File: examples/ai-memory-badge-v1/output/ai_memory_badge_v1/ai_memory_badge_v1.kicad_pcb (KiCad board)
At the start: 2 copper layers, 68 parts, among them J1 KH-TYPE-C-16P USB-C USB2.0 re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, J2 JST PH 2P SMD battery connect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, J3 U.FL/IPEX antenna connector, J4 UART debug 4P, J5 microSD socket push-push, M1 LCM0827A3038F 3V flat vibrati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, Q1 AO3400A NMOS low-side switch, SW1 Reset tactile switch, SW2 BOOT tactile switch, SW3 Mark tactile switch, SW4 Mute SPDT slide switch, U1 ESP32-S3R8 bare SoC, U2 AP2112K-3.3 600mA LDO, U3 MCP73831 LiPo charger, U4 W25Q128JVSIQ 16MB SPI flash, U5 8MB PSRAM reserve, DNP, U6 USB2.0 ESD protection, U7 I2C secure element, DNP, Y1 40MHz 12pF 10ppm crystal

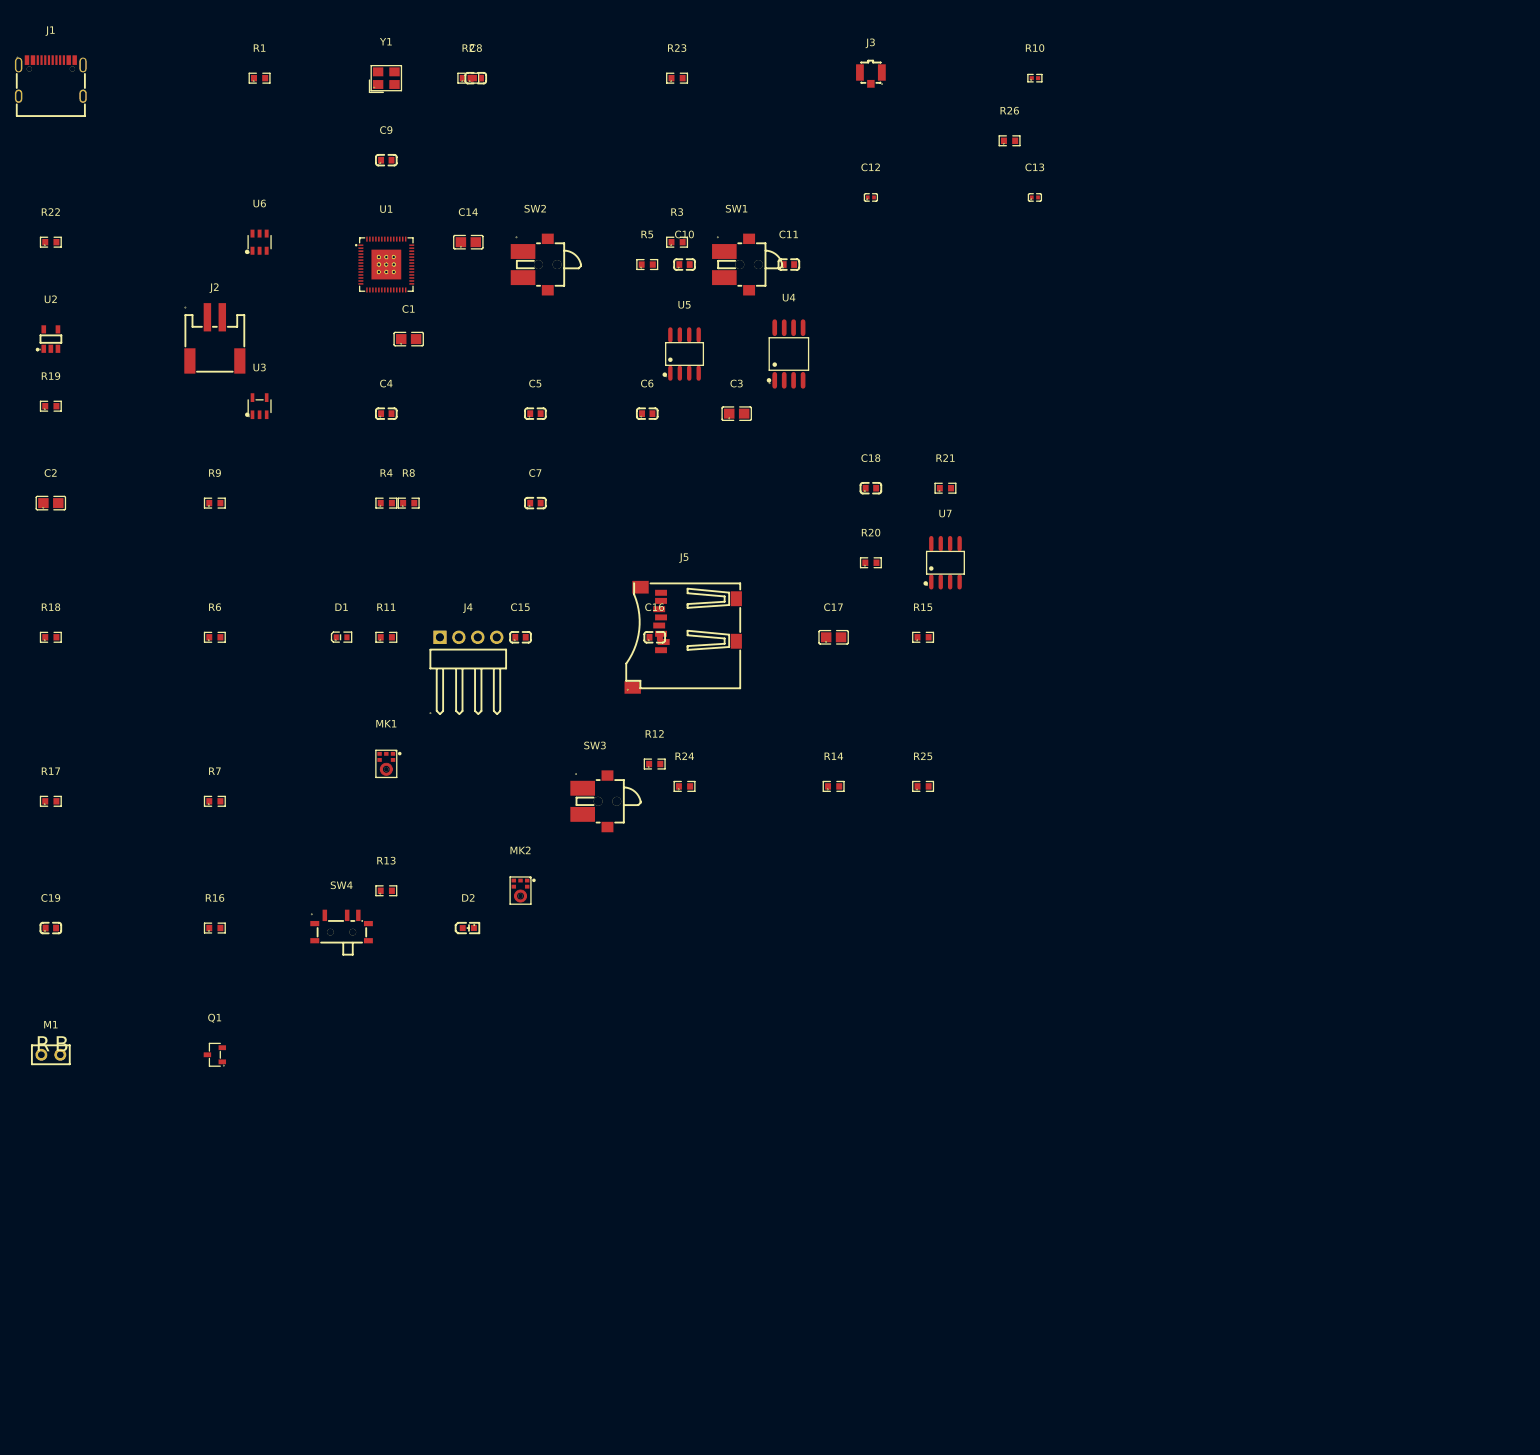
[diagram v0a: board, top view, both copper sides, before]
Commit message: refactor(example): rebuild ai-memory-badge with all topology fixes and optimizations
Circuit fixes:
- LED D1/D2 drive circuit corrected (GPIO controls LED via resistor)
- Mute switch redesigned (SPDT COM directly controls U9.ON)
- SYS_3V3 + EPD_3V3 merged for Rev A (J6.7 direct power)
- Removed J4 UART debug header, SW6 mode button, R16/R32 unused

Design optimizations:
- D3: BAT54C flyback diode across vibration motor M1
- C22: 100nF filter cap on VBAT_SENSE ADC input
- R24/R25: DNP (microSD CMD/DAT0 pullups unused in SPI mode)
- R11: mic power link connected to SYS_3V3
- R27/R28: corrected pullup/pulldown connections
- C20.1/C21.1: removed from SYS_3V3 (was shorting NFC antenna)
- R31.2/R32.2: removed from GND (was shorting button signals)
- J6.7/J7.2: fixed cross-net shorts

BOM consolidation:
- All passives unified to 0603 (was 0603+0805)
- SW4/SW5 unified to SMD SPDT slide switch (MST-12D18G4)
- SW1/SW2 moved to internal test sheet (not user-exposed)

3D models:
- 33 footprint files corrected to ${KIPRJMOD} relative paths
- New 3D models for downloaded components

Co-Authored-By: Claude <noreply@anthropic.com>
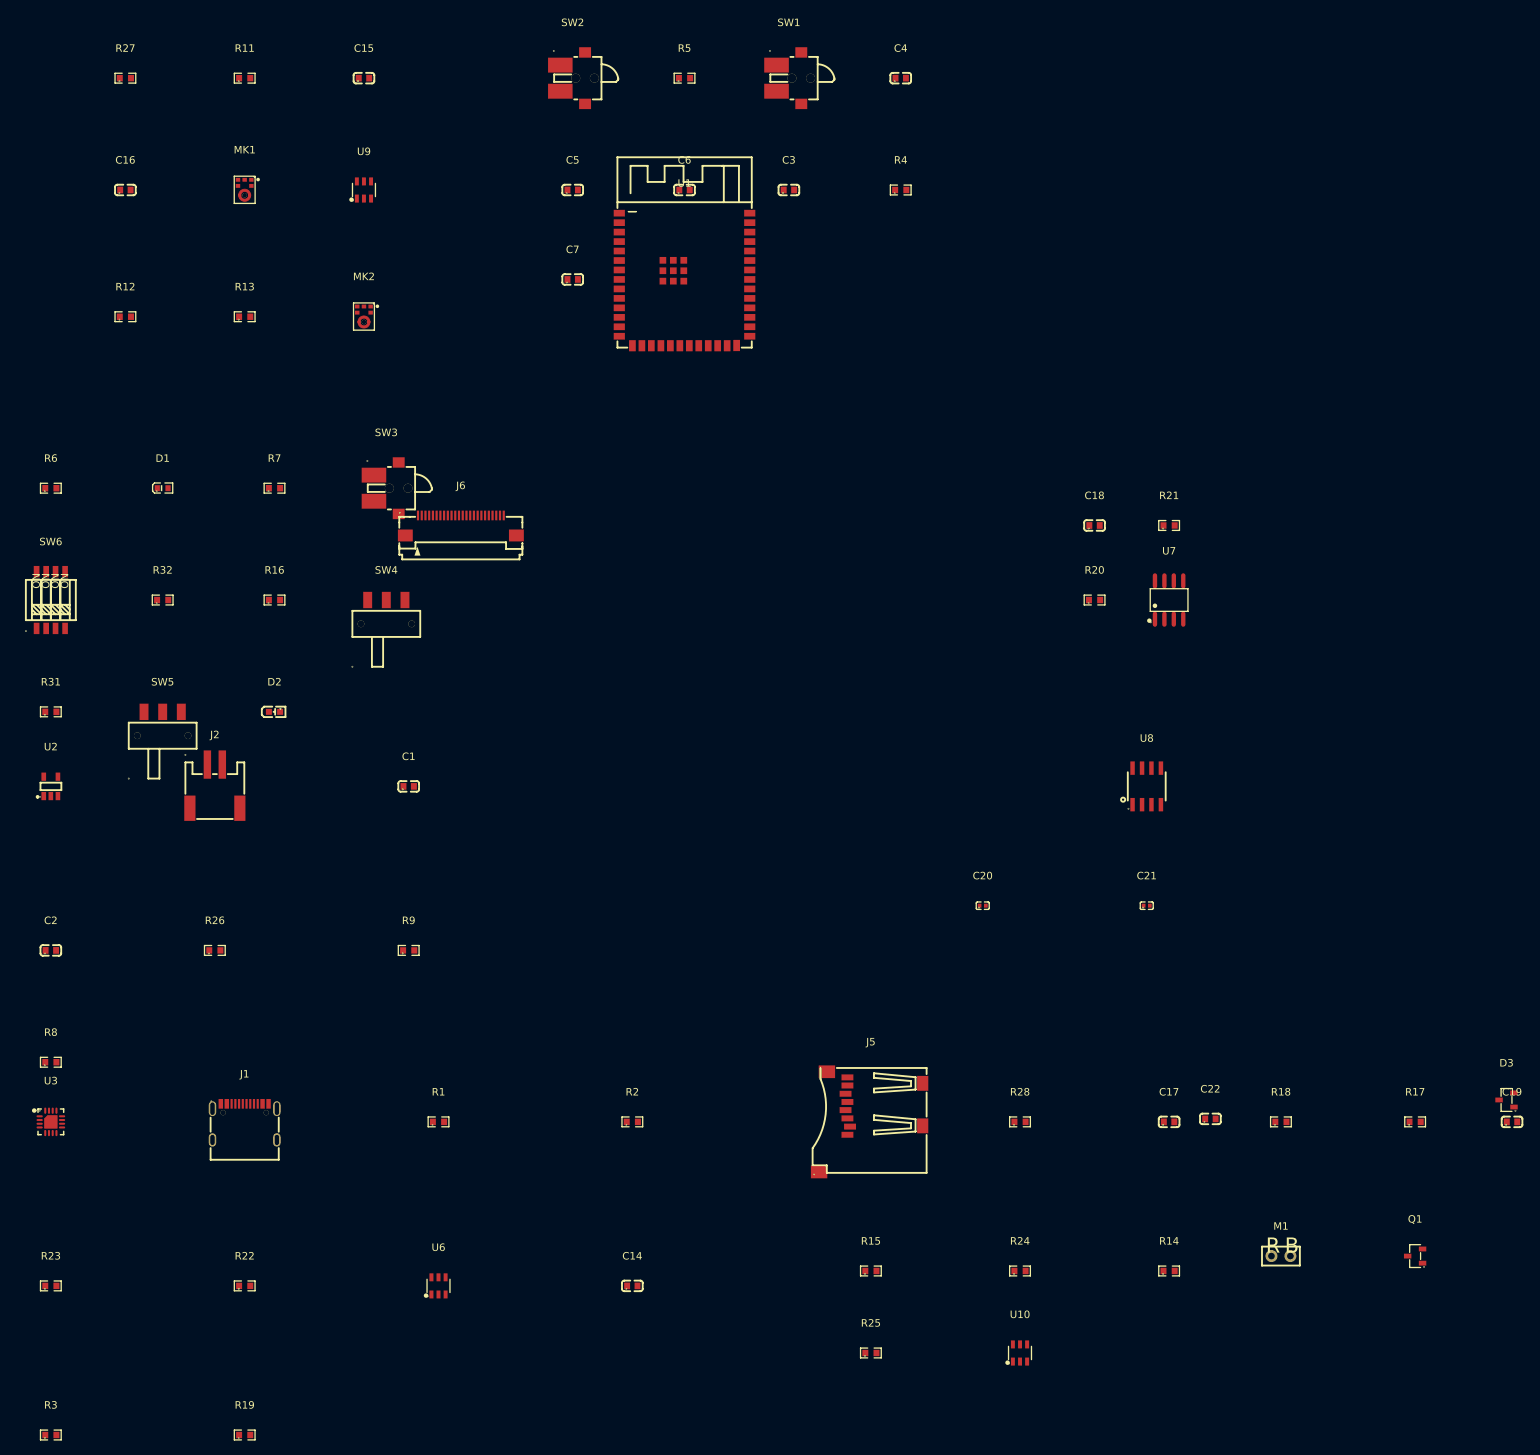
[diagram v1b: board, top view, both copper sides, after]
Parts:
- removed C10, C11: 100nF, C0603
- removed C12, C13: DNP, C0402
- removed C8, C9: 18pF, C0603
- removed J3: U.FL/IPEX antenna connector, RF-SMD_FRF05002-JSS103M
- removed J4: UART debug 4P, HDR-TH_4P-P2.54-H-M-W10.4
- removed R10: 0R, R0402
- removed U4: W25Q128JVSIQ 16MB SPI flash, SOIC-8_L5.3-W5.3-P1.27-LS8.0-BL
- removed U5: 8MB PSRAM reserve, DNP, SOIC-8_L4.9-W3.9-P1.27-LS6.0-BL
- removed Y1: 40MHz 12pF 10ppm crystal, CRYSTAL-SMD_4P-L3.2-W2.5-BL
- added C20: DNP, C0402, F.Cu at (135.0, 121.0)
- added C21: DNP, C0402, F.Cu at (157.0, 121.0)
- added C22: 100nF, C0603, F.Cu at (165.5, 149.6)
- added D3: BAT54 Schottky flyback, SOT-23-3_L2.9-W1.3-P1.90-LS2.4-BR, F.Cu at (205.3, 147.1)
- added J6: 2.13 inch black-white e-paper SPI connector, FPC-SMD_24P-P0.50-L6.1-W16.4, F.Cu at (65.0, 70.0)
- added R27: 10K, R0603, F.Cu at (20.0, 10.0)
- added R28: 100K, R0603, F.Cu at (140.0, 150.0)
- added R31: 10K, R0603, F.Cu at (10.0, 95.0)
- added R32: 10K, R0603, F.Cu at (25.0, 80.0)
- added SW5: REC slide switch SPDT, SW-SMD_MST-12D18G4-SPDT-SLIDE-SWITCH, F.Cu at (25.0, 95.0)
- added SW6: MODE side tactile button, SW-SMD_8P-L6.7-W5.4-P1.27-LS8.4, F.Cu at (10.0, 80.0)
- added U10: TPS22918 SD_3V3 load switch, SOT-23-6_L2.9-W1.6-P0.95-LS2.8-BL, F.Cu at (140.0, 181.0)
- added U8: ST25DV04KC dynamic NFC tag, SO-8_L4.9-W3.9-P1.27-LS6.0-BL, F.Cu at (157.0, 105.0)
- added U9: TPS22918 MIC_3V3 load switch, SOT-23-6_L2.9-W1.6-P0.95-LS2.8-BL, F.Cu at (52.0, 25.0)
- C1, C14, C17, C2, C3: footprint C0805 -> C0603
- SW4: footprint SW-TH_MSK12C02-HB-1 -> SW-SMD_MST-12D18G4-SPDT-SLIDE-SWITCH
- U1: value ESP32-S3R8 bare SoC -> ESP32-S3-WROOM-1-N8R8 module; footprint QFN-56_L7.0-W7.0-P0.40-TL-EP4.0 -> WIRELM-SMD_ESP32-S3-WROOM-1
- U3: value MCP73831 LiPo charger -> BQ24074 LiPo charger with power-path; footprint SOT-23-5_L3.0-W1.7-P0.95-LS2.8-BL -> QFN-16_L3.0-W3.0-P0.50-TL-EP1.7
- moved C19 197.7 mm to (206.0, 150.0)
- moved R17 188.0 mm to (193.0, 150.0)
- moved R23 182.5 mm to (10.0, 172.0)
- moved R3 180.7 mm to (10.0, 192.0)
- moved R18 177.3 mm to (175.0, 150.0)
- moved M1 167.2 mm to (175.0, 168.0)
- moved Q1 163.2 mm to (193.0, 168.0)
- moved R26 152.2 mm to (32.0, 127.0)
- moved J1 142.4 mm to (36.0, 150.0)
- moved R22 142.4 mm to (36.0, 172.0)
- moved R1 142.0 mm to (62.0, 150.0)
- moved U6 142.0 mm to (62.0, 172.0)
- moved C14 141.7 mm to (88.0, 172.0)
- moved R2 141.7 mm to (88.0, 150.0)
- moved R19 140.4 mm to (36.0, 192.0)
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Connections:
- C1 pad 1: BAT_P -> VSYS
- C17 pad 1: SYS_3V3 -> SD_3V3
- D1 pad 1: (no net) -> LED_POWER
- D1 pad 2: (no net) -> SYS_3V3
- D2 pad 1: (no net) -> SYS_3V3
- D2 pad 2: (no net) -> LED_RECORD
- J5 pad 4: (no net) -> SD_3V3
- J5 pad 6: (no net) -> GND
- MK1 pad 1: (no net) -> MIC_3V3
- MK1 pad 2: (no net) -> I2S_BCLK
- MK1 pad 3: (no net) -> GND
- MK1 pad 4: (no net) -> MIC_LR_SEL_L
- MK1 pad 5: (no net) -> I2S_LRCLK
- MK1 pad 6: (no net) -> I2S_DIN
- MK2 pad 1: (no net) -> MIC_3V3
- MK2 pad 2: (no net) -> I2S_BCLK
- MK2 pad 3: (no net) -> GND
- MK2 pad 4: (no net) -> MIC_LR_SEL_R
- MK2 pad 5: (no net) -> I2S_LRCLK
- MK2 pad 6: (no net) -> I2S_DIN
- Q1 pad 1: (no net) -> MOTOR_GATE
- Q1 pad 2: (no net) -> GND
- Q1 pad 3: (no net) -> MOTOR_LOW
- R14 pad 1: SYS_3V3 -> SD_3V3
- R15 pad 1: SYS_3V3 -> SD_3V3
- R16 pad 1: SYS_3V3 -> (no net)
- R16 pad 2: SW_MUTE -> (no net)
- R24 pad 1: SYS_3V3 -> SD_3V3
- R25 pad 1: SYS_3V3 -> SD_3V3
- R6 pad 2: GND -> LED_POWER_DRV
- R7 pad 2: GND -> LED_RECORD_DRV
- R8 pad 1: BAT_P -> VSYS
- SW4 pad 1: SW_MUTE -> MIC_PWR_EN
- SW4 pad 2: GND -> MIC_PWR_NC
- U1 pad 1: (no net) -> GND
- U1 pad 10: (no net) -> MIC_PWR_EN
- U1 pad 11: (no net) -> MOTOR_DRV
- U1 pad 12: (no net) -> SD_CS
- U1 pad 13: (no net) -> USB_D_N
- U1 pad 14: (no net) -> USB_D_P
- U1 pad 17: (no net) -> SD_MISO
- U1 pad 18: (no net) -> SD_SCLK
- U1 pad 19: (no net) -> SD_MOSI
- U1 pad 2: (no net) -> SYS_3V3
- U1 pad 20: (no net) -> I2S_BCLK
- U1 pad 21: (no net) -> I2S_LRCLK
- U1 pad 22: (no net) -> I2S_DIN
- U1 pad 23: (no net) -> I2C_SDA
- U1 pad 27: (no net) -> ESP_BOOT
- U1 pad 28: (no net) -> EPD_CS
- U1 pad 29: (no net) -> EPD_DC
- U1 pad 3: (no net) -> ESP_EN
- U1 pad 30: (no net) -> EPD_RST
- U1 pad 31: (no net) -> EPD_BUSY
- U1 pad 32: (no net) -> REC_BTN
- U1 pad 33: (no net) -> MODE_BTN
- U1 pad 34: (no net) -> NFC_GPO
- U1 pad 36: (no net) -> UART0_RX
- U1 pad 37: (no net) -> UART0_TX
- U1 pad 38: (no net) -> LED_POWER_DRV
- U1 pad 39: (no net) -> VBAT_SENSE
- U1 pad 4: (no net) -> LED_RECORD_DRV
- U1 pad 5: (no net) -> I2C_SCL
- U1 pad 6: (no net) -> BTN_MARK
- U1 pad 7: (no net) -> SD_CD
- U1 pad 8: (no net) -> EPD_PWR_EN
- U1 pad 9: (no net) -> SD_PWR_EN
- U2 pad 1: (no net) -> VSYS
- U2 pad 2: (no net) -> GND
- U2 pad 3: (no net) -> VSYS
- U2 pad 5: (no net) -> SYS_3V3_REG
- U3 pad 2: (no net) -> BAT_P
- U7 pad 4: (no net) -> GND
- U7 pad 5: (no net) -> I2C_SDA
- U7 pad 6: (no net) -> I2C_SCL
- U7 pad 8: (no net) -> SYS_3V3

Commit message: feat(example): 重建 ai-memory-badge 输出项目, 添加交接文档和 ERC 报告
Rebuild ai-memory-badge output project, add handoff doc and ERC reports

- 重新生成 .kicad_pro/.kicad_sch/.kicad_pcb/.kicad_prl 全套 KiCad 文件
- 更新输出目录中的 JLC-MCP 符号库和封装库 (镜像 source/libraries/)
- 新增 ERC 验证报告 (erc.json + erc.summary.json)
- 新增 kicad-execution-plan.json 和 jlc-mcp-install-report.json
- 新增 AIAgent.pretty 自定义封装目录
- 新增 pipeline-events.jsonl / simulation-*.json 流水线产物
- 删除残留锁文件 ~ai_memory_badge_v1.kicad_pro.lck
- 添加 HANDOFF.md 项目交接文档 (硬件架构/BOM 统计/文件结构/已知问题/投板清单)

Co-Authored-By: Claude <noreply@anthropic.com>
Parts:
- removed C20, C21: DNP, C0402
- removed R16, R24, R25, R32: 10K, R0603
- removed SW6: MODE side tactile button, SW-SMD_8P-L6.7-W5.4-P1.27-LS8.4
- removed U7: I2C secure element, DNP, SOIC-8_L4.9-W3.9-P1.27-LS6.0-BL
- SW1: value Reset tactile switch -> Reset pushbutton
- SW2: value BOOT tactile switch -> BOOT pushbutton
- moved D3 127.7 mm to (168.8, 24.6)
- moved C22 125.7 mm to (178.8, 24.6)
- moved SW3 47.4 mm to (10.0, 80.0)
- moved R31 33.5 mm to (40.0, 80.0)
- moved SW4 30.0 mm to (25.0, 80.0)
- moved U10 22.8 mm to (160.0, 170.0)
- moved R14 20.0 mm to (140.0, 170.0)
- moved D2 15.0 mm to (25.0, 95.0)
- moved SW5 15.0 mm to (10.0, 95.0)
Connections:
- U1 pad 24: (no net) -> EPD_SCLK
- U1 pad 25: (no net) -> EPD_MOSI
- U10 pad 1: (no net) -> SYS_3V3
- U10 pad 6: (no net) -> SD_3V3
- U3 pad 16: (no net) -> CHG_PROG
- U3 pad 9: (no net) -> CHG_STAT
- U9 pad 1: (no net) -> SYS_3V3
- U9 pad 6: (no net) -> MIC_3V3
